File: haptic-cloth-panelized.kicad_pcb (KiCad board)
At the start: 2 copper layers, 102 x 88 mm, 568 parts, among them J1 Conn_01x03, J2 Conn_01x03, J3 Prog, M1 Motor_DC, Q1 BSS138, U1 PFS172-SO8

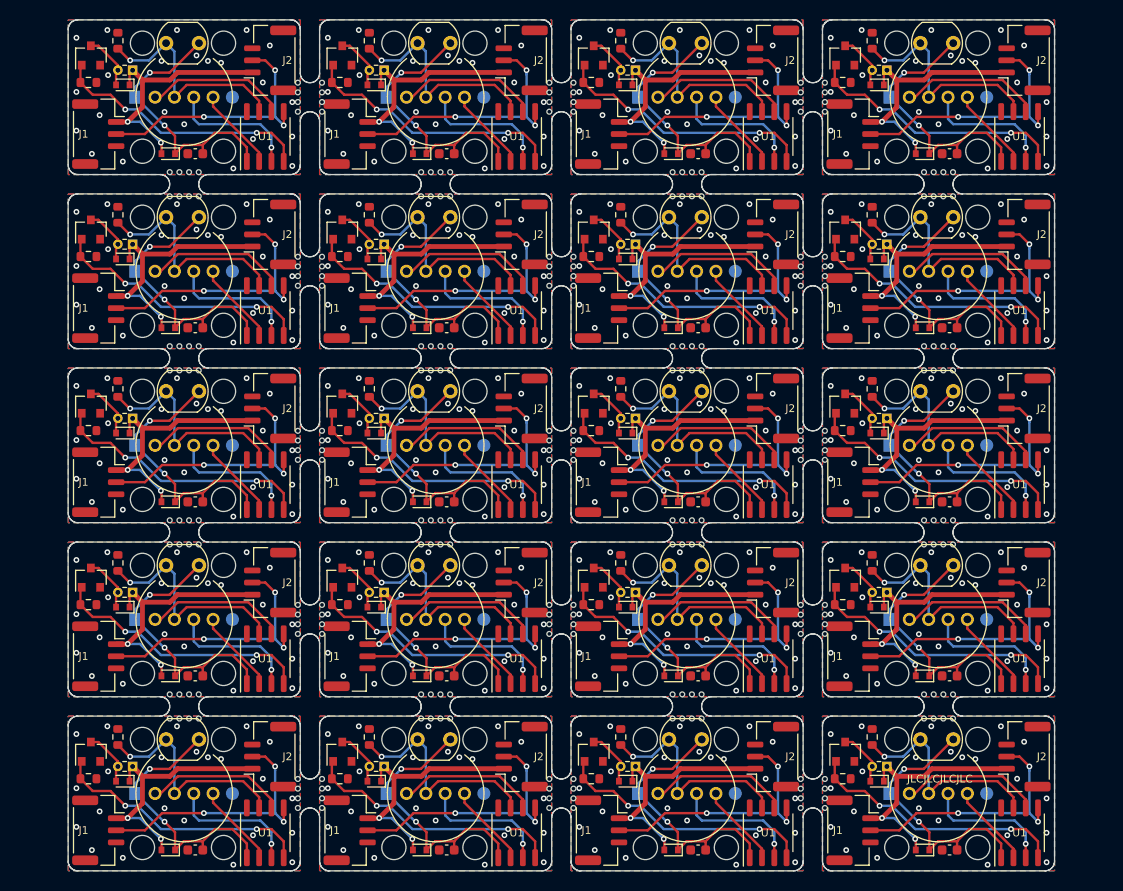
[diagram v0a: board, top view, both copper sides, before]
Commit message: Shift motor connector further away
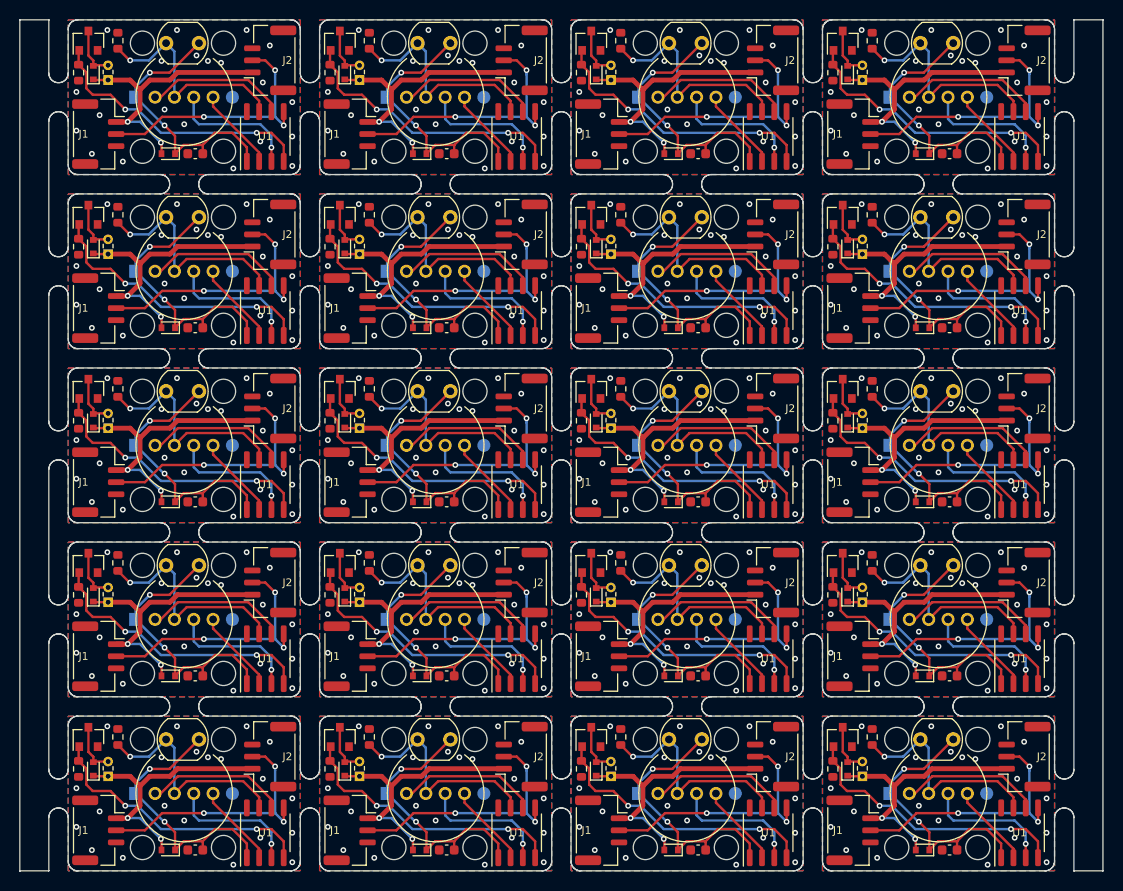
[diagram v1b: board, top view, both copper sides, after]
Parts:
- removed the D1 at (133.7, 128.7)
- removed the D1 at (107.7, 92.7)
- removed the D1 at (81.7, 92.7)
- removed the D1 at (55.7, 92.7)
- removed the D1 at (133.7, 74.7)
- removed the D1 at (107.7, 74.7)
- removed the D1 at (81.7, 74.7)
- removed the D1 at (55.7, 74.7)
- removed the D1 at (133.7, 56.7)
- removed the D1 at (107.7, 56.7)
- removed the D1 at (81.7, 56.7)
- removed the D1 at (107.7, 128.7)
- removed the D1 at (55.7, 56.7)
- removed the D1 at (81.7, 128.7)
- removed the D1 at (55.7, 128.7)
- removed the D1 at (133.7, 110.7)
- removed the D1 at (107.7, 110.7)
- removed the D1 at (81.7, 110.7)
- removed the D1 at (55.7, 110.7)
- removed the D1 at (133.7, 92.7)
- removed the M1 at (133.9, 127.2)
- removed the M1 at (107.9, 91.2)
- removed the M1 at (81.9, 91.2)
- removed the M1 at (55.9, 91.2)
- removed the M1 at (133.9, 73.2)
- removed the M1 at (107.9, 73.2)
- removed the M1 at (81.9, 73.2)
- removed the M1 at (55.9, 73.2)
- removed the M1 at (133.9, 55.2)
- removed the M1 at (107.9, 55.2)
- removed the M1 at (81.9, 55.2)
- removed the M1 at (107.9, 127.2)
- removed the M1 at (55.9, 55.2)
- removed the M1 at (81.9, 127.2)
- removed the M1 at (55.9, 127.2)
- removed the M1 at (133.9, 109.2)
- removed the M1 at (107.9, 109.2)
- removed the M1 at (81.9, 109.2)
- removed the M1 at (55.9, 109.2)
- removed the M1 at (133.9, 91.2)
- removed the Q1 at (130.3, 125.7)
- removed the Q1 at (104.3, 89.7)
- removed the Q1 at (78.3, 89.7)
- removed the Q1 at (52.3, 89.7)
- removed the Q1 at (130.3, 71.7)
- removed the Q1 at (104.3, 71.7)
- removed the Q1 at (78.3, 71.7)
- removed the Q1 at (52.3, 71.7)
- removed the Q1 at (130.3, 53.7)
- removed the Q1 at (104.3, 53.7)
- removed the Q1 at (78.3, 53.7)
- removed the Q1 at (104.3, 125.7)
- removed the Q1 at (52.3, 53.7)
- removed the Q1 at (78.3, 125.7)
- removed the Q1 at (52.3, 125.7)
- removed the Q1 at (130.3, 107.7)
- removed the Q1 at (104.3, 107.7)
- removed the Q1 at (78.3, 107.7)
- removed the Q1 at (52.3, 107.7)
- removed the Q1 at (130.3, 89.7)
- removed the R3 at (130.1, 128.5)
- removed the R3 at (104.1, 92.5)
- removed the R3 at (78.1, 92.5)
- removed the R3 at (52.1, 92.5)
- removed the R3 at (130.1, 74.5)
- removed the R3 at (104.1, 74.5)
- removed the R3 at (78.1, 74.5)
- removed the R3 at (52.1, 74.5)
- removed the R3 at (130.1, 56.5)
- removed the R3 at (104.1, 56.5)
- removed the R3 at (78.1, 56.5)
- removed the R3 at (104.1, 128.5)
- removed the R3 at (52.1, 56.5)
- removed the R3 at (78.1, 128.5)
- removed the R3 at (52.1, 128.5)
- removed the R3 at (130.1, 110.5)
- removed the R3 at (104.1, 110.5)
- removed the R3 at (78.1, 110.5)
- removed the R3 at (52.1, 110.5)
- removed the R3 at (130.1, 92.5)
- removed REF** (x248): NPTH, NPTH
- added D1: 1N5819, Diode_SMD:D_SOD-523, F.Cu at (130.6, 127.5)
- added D1: 1N5819, Diode_SMD:D_SOD-523, F.Cu at (104.6, 91.5)
- added D1: 1N5819, Diode_SMD:D_SOD-523, F.Cu at (78.6, 91.5)
- added D1: 1N5819, Diode_SMD:D_SOD-523, F.Cu at (52.6, 91.5)
- added D1: 1N5819, Diode_SMD:D_SOD-523, F.Cu at (130.6, 73.5)
- added D1: 1N5819, Diode_SMD:D_SOD-523, F.Cu at (104.6, 73.5)
- added D1: 1N5819, Diode_SMD:D_SOD-523, F.Cu at (78.6, 73.5)
- added D1: 1N5819, Diode_SMD:D_SOD-523, F.Cu at (52.6, 73.5)
- added D1: 1N5819, Diode_SMD:D_SOD-523, F.Cu at (130.6, 55.5)
- added D1: 1N5819, Diode_SMD:D_SOD-523, F.Cu at (104.6, 55.5)
- added D1: 1N5819, Diode_SMD:D_SOD-523, F.Cu at (78.6, 55.5)
- added D1: 1N5819, Diode_SMD:D_SOD-523, F.Cu at (104.6, 127.5)
- added D1: 1N5819, Diode_SMD:D_SOD-523, F.Cu at (52.6, 55.5)
- added D1: 1N5819, Diode_SMD:D_SOD-523, F.Cu at (78.6, 127.5)
- added D1: 1N5819, Diode_SMD:D_SOD-523, F.Cu at (52.6, 127.5)
- added D1: 1N5819, Diode_SMD:D_SOD-523, F.Cu at (130.6, 109.5)
- added D1: 1N5819, Diode_SMD:D_SOD-523, F.Cu at (104.6, 109.5)
- added D1: 1N5819, Diode_SMD:D_SOD-523, F.Cu at (78.6, 109.5)
- added D1: 1N5819, Diode_SMD:D_SOD-523, F.Cu at (52.6, 109.5)
- added D1: 1N5819, Diode_SMD:D_SOD-523, F.Cu at (130.6, 91.5)
- added M1: Motor_DC, haptic-cloth:Motor, F.Cu at (132.1, 127.5)
- added M1: Motor_DC, haptic-cloth:Motor, F.Cu at (106.1, 91.5)
- added M1: Motor_DC, haptic-cloth:Motor, F.Cu at (80.1, 91.5)
- added M1: Motor_DC, haptic-cloth:Motor, F.Cu at (54.1, 91.5)
- added M1: Motor_DC, haptic-cloth:Motor, F.Cu at (132.1, 73.5)
- added M1: Motor_DC, haptic-cloth:Motor, F.Cu at (106.1, 73.5)
- added M1: Motor_DC, haptic-cloth:Motor, F.Cu at (80.1, 73.5)
- added M1: Motor_DC, haptic-cloth:Motor, F.Cu at (54.1, 73.5)
- added M1: Motor_DC, haptic-cloth:Motor, F.Cu at (132.1, 55.5)
- added M1: Motor_DC, haptic-cloth:Motor, F.Cu at (106.1, 55.5)
- added M1: Motor_DC, haptic-cloth:Motor, F.Cu at (80.1, 55.5)
- added M1: Motor_DC, haptic-cloth:Motor, F.Cu at (106.1, 127.5)
- added M1: Motor_DC, haptic-cloth:Motor, F.Cu at (54.1, 55.5)
- added M1: Motor_DC, haptic-cloth:Motor, F.Cu at (80.1, 127.5)
- added M1: Motor_DC, haptic-cloth:Motor, F.Cu at (54.1, 127.5)
- added M1: Motor_DC, haptic-cloth:Motor, F.Cu at (132.1, 109.5)
- added M1: Motor_DC, haptic-cloth:Motor, F.Cu at (106.1, 109.5)
- added M1: Motor_DC, haptic-cloth:Motor, F.Cu at (80.1, 109.5)
- added M1: Motor_DC, haptic-cloth:Motor, F.Cu at (54.1, 109.5)
- added M1: Motor_DC, haptic-cloth:Motor, F.Cu at (132.1, 91.5)
- added Q1: BSS138, Package_TO_SOT_SMD:SOT-23, F.Cu at (130.1, 124.2)
- added Q1: BSS138, Package_TO_SOT_SMD:SOT-23, F.Cu at (104.1, 88.2)
- added Q1: BSS138, Package_TO_SOT_SMD:SOT-23, F.Cu at (78.1, 88.2)
- added Q1: BSS138, Package_TO_SOT_SMD:SOT-23, F.Cu at (52.1, 88.2)
- added Q1: BSS138, Package_TO_SOT_SMD:SOT-23, F.Cu at (130.1, 70.2)
- added Q1: BSS138, Package_TO_SOT_SMD:SOT-23, F.Cu at (104.1, 70.2)
- added Q1: BSS138, Package_TO_SOT_SMD:SOT-23, F.Cu at (78.1, 70.2)
- added Q1: BSS138, Package_TO_SOT_SMD:SOT-23, F.Cu at (52.1, 70.2)
- added Q1: BSS138, Package_TO_SOT_SMD:SOT-23, F.Cu at (130.1, 52.2)
- added Q1: BSS138, Package_TO_SOT_SMD:SOT-23, F.Cu at (104.1, 52.2)
- added Q1: BSS138, Package_TO_SOT_SMD:SOT-23, F.Cu at (78.1, 52.2)
- added Q1: BSS138, Package_TO_SOT_SMD:SOT-23, F.Cu at (104.1, 124.2)
- added Q1: BSS138, Package_TO_SOT_SMD:SOT-23, F.Cu at (52.1, 52.2)
- added Q1: BSS138, Package_TO_SOT_SMD:SOT-23, F.Cu at (78.1, 124.2)
- added Q1: BSS138, Package_TO_SOT_SMD:SOT-23, F.Cu at (52.1, 124.2)
- added Q1: BSS138, Package_TO_SOT_SMD:SOT-23, F.Cu at (130.1, 106.2)
- added Q1: BSS138, Package_TO_SOT_SMD:SOT-23, F.Cu at (104.1, 106.2)
- added Q1: BSS138, Package_TO_SOT_SMD:SOT-23, F.Cu at (78.1, 106.2)
- added Q1: BSS138, Package_TO_SOT_SMD:SOT-23, F.Cu at (52.1, 106.2)
- added Q1: BSS138, Package_TO_SOT_SMD:SOT-23, F.Cu at (130.1, 88.2)
- added R3: 47k, Resistor_SMD:R_0603_1608Metric, F.Cu at (129.1, 127.5)
- added R3: 47k, Resistor_SMD:R_0603_1608Metric, F.Cu at (103.1, 91.5)
- added R3: 47k, Resistor_SMD:R_0603_1608Metric, F.Cu at (77.1, 91.5)
- added R3: 47k, Resistor_SMD:R_0603_1608Metric, F.Cu at (51.1, 91.5)
- added R3: 47k, Resistor_SMD:R_0603_1608Metric, F.Cu at (129.1, 73.5)
- added R3: 47k, Resistor_SMD:R_0603_1608Metric, F.Cu at (103.1, 73.5)
- added R3: 47k, Resistor_SMD:R_0603_1608Metric, F.Cu at (77.1, 73.5)
- added R3: 47k, Resistor_SMD:R_0603_1608Metric, F.Cu at (51.1, 73.5)
- added R3: 47k, Resistor_SMD:R_0603_1608Metric, F.Cu at (129.1, 55.5)
- added R3: 47k, Resistor_SMD:R_0603_1608Metric, F.Cu at (103.1, 55.5)
- added R3: 47k, Resistor_SMD:R_0603_1608Metric, F.Cu at (77.1, 55.5)
- added R3: 47k, Resistor_SMD:R_0603_1608Metric, F.Cu at (103.1, 127.5)
- added R3: 47k, Resistor_SMD:R_0603_1608Metric, F.Cu at (51.1, 55.5)
- added R3: 47k, Resistor_SMD:R_0603_1608Metric, F.Cu at (77.1, 127.5)
- added R3: 47k, Resistor_SMD:R_0603_1608Metric, F.Cu at (51.1, 127.5)
- added R3: 47k, Resistor_SMD:R_0603_1608Metric, F.Cu at (129.1, 109.5)
- added R3: 47k, Resistor_SMD:R_0603_1608Metric, F.Cu at (103.1, 109.5)
- added R3: 47k, Resistor_SMD:R_0603_1608Metric, F.Cu at (77.1, 109.5)
- added R3: 47k, Resistor_SMD:R_0603_1608Metric, F.Cu at (51.1, 109.5)
- added R3: 47k, Resistor_SMD:R_0603_1608Metric, F.Cu at (129.1, 91.5)
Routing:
- net Board_8-VCC: track 26.2 -> 28.2 mm
- net Board_16-VCC: track 26.2 -> 28.2 mm
- net Board_7-VCC: track 26.2 -> 28.2 mm
- net Board_20-VCC: track 26.2 -> 28.2 mm
- net Board_15-VCC: track 26.2 -> 28.2 mm
- net Board_4-VCC: track 26.2 -> 28.2 mm
- net Board_12-VCC: track 26.2 -> 28.2 mm
- net Board_19-VCC: track 26.2 -> 28.2 mm
- net Board_5-VCC: track 26.2 -> 28.2 mm
- net Board_3-VCC: track 26.2 -> 28.2 mm
- net Board_17-VCC: track 26.2 -> 28.2 mm
- net Board_13-VCC: track 26.2 -> 28.2 mm
- net Board_11-VCC: track 26.2 -> 28.2 mm
- net Board_9-VCC: track 26.2 -> 28.2 mm
- net Board_1-VCC: track 26.2 -> 28.2 mm
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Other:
- board size 102 x 88 mm -> 112 x 88 mm
- board text removed: "JLCJLCJLCJLC"
